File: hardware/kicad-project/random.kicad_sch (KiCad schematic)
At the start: 33 parts, among them J7 Conn_01x50, Q3 DMG2301L-7, SW1 K2-1109SP-C4SA, SW2 K2-1109SP-C4SA, SW3 K2-1109SP-C4SA, SW4 K2-1109SP-C4SA, SW5 GT-TC054C-H035-L1W, SW6 GT-TC054C-H035-L1W, SW7 GT-TC054C-H035-L1W

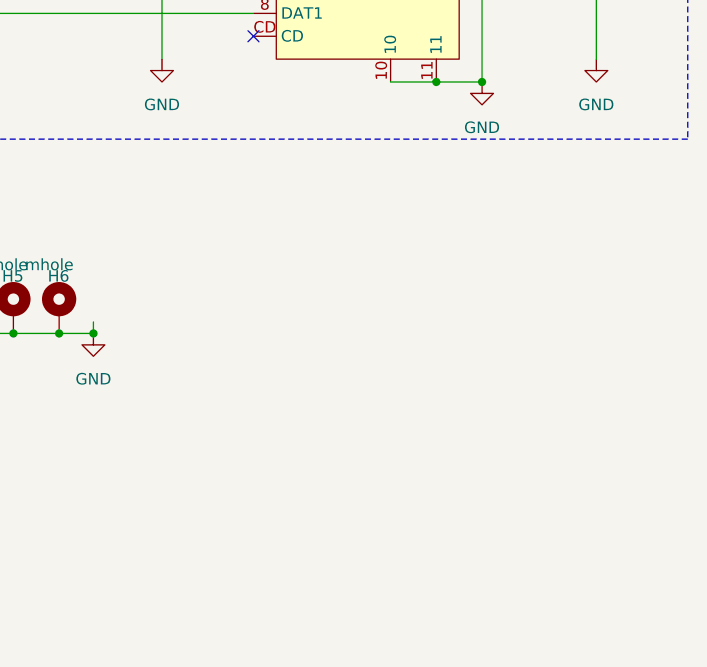
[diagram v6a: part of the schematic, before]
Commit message: change of LDO in schematics
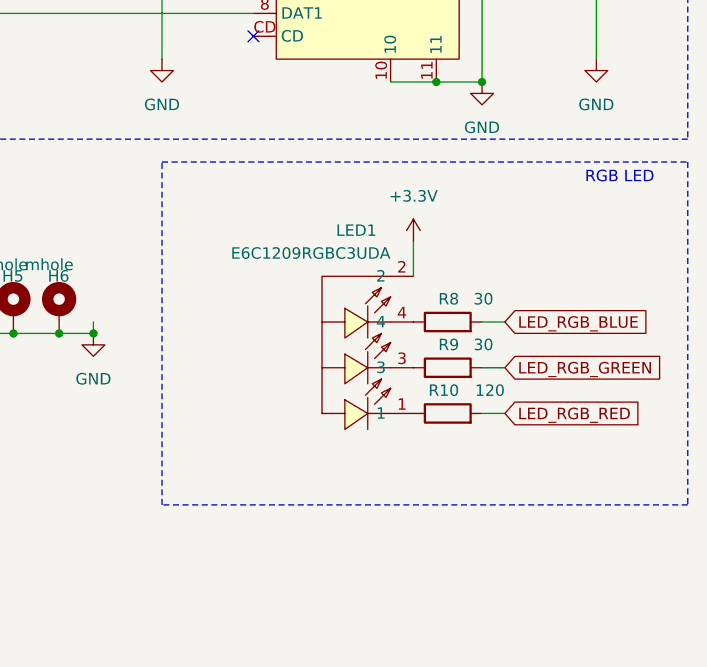
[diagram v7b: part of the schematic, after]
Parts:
- added LED1: E6C1209RGBC3UDA, easyeda2kicad:LED-ARRAY-SMD_4P-L3.2-W2.7-TL-1, symbol easyedaToKicad:E6C1209RGBC3UDA
- added R10: 120, Resistor_SMD:R_0805_2012Metric, symbol Device:R
- added R8, R9: 30, Resistor_SMD:R_0805_2012Metric, symbol Device:R
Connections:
- net +3.3V: now also LED1.2
- new net: LED1.4, R8.1
- new net: LED1.1, R10.1
- new net: LED1.3, R9.1
- new net LED_RGB_BLUE: R8.2
- new net LED_RGB_GREEN: R9.2
- new net LED_RGB_RED: R10.2
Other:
- note added: "RGB LED"
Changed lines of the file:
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@@
+    (stroke (width 0) (type default))
+  )
+  (wire (pts (xy 251.46 81.28) (xy 251.46 85.09))
     (stroke (width 0) (type default))
   )
@@
     (stroke (width 0) (type default))
   )
+  (wire (pts (xy 259.08 90.17) (xy 261.62 90.17))
+    (stroke (width 0) (type default))
+  )
   (wire (pts (xy 196.85 35.56) (xy 196.85 55.88))
     (stroke (width 0) (type default))
@@
   )
   (wire (pts (xy 223.52 60.96) (xy 223.52 50.8))
+    (stroke (width 0) (type default))
+  )
+  (wire (pts (xy 259.08 100.33) (xy 261.62 100.33))
     (stroke (width 0) (type default))
   )
@@
   )
   (wire (pts (xy 31.75 143.51) (xy 31.75 158.75))
+    (stroke (width 0) (type default))
+  )
+  (wire (pts (xy 259.08 95.25) (xy 261.62 95.25))
     (stroke (width 0) (type default))
   )
@@
     (fill (type none))
   )
+  (rectangle (start 223.52 72.39) (end 281.94 110.49)
+    (stroke (width 0) (type dash))
+    (fill (type none))
+  )
   (text "DB1" (at 106.68 125.73 0)
     (effects (font (size 1.27 1.27)) (justify left bottom))
@@
   )
   (text "DB0" (at 106.68 128.27 0)
+    (effects (font (size 1.27 1.27)) (justify left bottom))
+  )
+  (text "RGB LED\n" (at 270.51 74.93 0)
     (effects (font (size 1.27 1.27)) (justify left bottom))
   )
@@
     )
   )
+  (global_label "LED_RGB_RED" (shape input) (at 261.62 100.33 0) (fields_autoplaced)
+    (effects (font (size 1.27 1.27)) (justify left))
+    (property "Intersheetrefs" "${INTERSHEET_REFS}" (at 277.4865 100.33 0)
+      (effects (font (size 1.27 1.27)) (justify left) hide)
+    )
+  )
+  (global_label "LED_RGB_BLUE" (shape input) (at 261.62 90.17 0) (fields_autoplaced)
+    (effects (font (size 1.27 1.27)) (justify left))
+    (property "Intersheetrefs" "${INTERSHEET_REFS}" (at 278.5751 90.17 0)
+      (effects (font (size 1.27 1.27)) (justify left) hide)
+    )
+  )
   (global_label "SD_DAT_2" (shape input) (at 190.5 38.1 180) (fields_autoplaced)
     (effects (font (size 1.27 1.27)) (justify right))
@@
     )
   )
+  (global_label "LED_RGB_GREEN" (shape input) (at 261.62 95.25 0) (fields_autoplaced)
+    (effects (font (size 1.27 1.27)) (justify left))
+    (property "Intersheetrefs" "${INTERSHEET_REFS}" (at 279.966 95.25 0)
+      (effects (font (size 1.27 1.27)) (justify left) hide)
+    )
+  )
   (global_label "BTN_1" (shape input) (at 135.89 29.21 180) (fields_autoplaced)
     (effects (font (size 1.27 1.27)) (justify right))
@@
     )
   )
+  (symbol (lib_id "Device:R") (at 255.27 90.17 90) (unit 1)
+    (in_bom yes) (on_board yes) (dnp no)
+    (property "Reference" "R8" (at 256.54 87.63 90)
+      (effects (font (size 1.27 1.27)) (justify left))
+    )
+    (property "Value" "30" (at 260.35 87.63 90)
+      (effects (font (size 1.27 1.27)) (justify left))
+    )
+    (property "Footprint" "Resistor_SMD:R_0805_2012Metric" (at 255.27 91.948 90)
+      (effects (font (size 1.27 1.27)) hide)
+    )
+    (property "Datasheet" "~" (at 255.27 90.17 0)
+      (effects (font (size 1.27 1.27)) hide)
+    )
+    (pin "1")
+    (pin "2")
+    (instances
+      (project "Untitled"
+        (path "/0de5ae84-7f75-4a5a-83a1-35d27fd1d8d2"
+          (reference "R8") (unit 1)
+        )
+        (path "/0de5ae84-7f75-4a5a-83a1-35d27fd1d8d2/7a3aed0a-25fa-4aa7-ba6a-02a8683cfb94"
+          (reference "R8") (unit 1)
+        )
+      )
+    )
+  )
   (symbol (lib_id "Device:C") (at 52.07 52.07 0) (mirror x) (unit 1)
     (in_bom yes) (on_board yes) (dnp no)
@@
         (path "/0de5ae84-7f75-4a5a-83a1-35d27fd1d8d2/7a3aed0a-25fa-4aa7-ba6a-02a8683cfb94"
           (reference "#PWR019") (unit 1)
+        )
+      )
+    )
+  )
+  (symbol (lib_id "power:+3.3V") (at 251.46 81.28 0) (unit 1)
+    (in_bom yes) (on_board yes) (dnp no) (fields_autoplaced)
+    (property "Reference" "#PWR026" (at 251.46 85.09 0)
+      (effects (font (size 1.27 1.27)) hide)
+    )
+    (property "Value" "+3.3V" (at 251.46 76.2 0)
+      (effects (font (size 1.27 1.27)))
+    )
+    (property "Footprint" "" (at 251.46 81.28 0)
+      (effects (font (size 1.27 1.27)) hide)
+    )
+    (property "Datasheet" "" (at 251.46 81.28 0)
+      (effects (font (size 1.27 1.27)) hide)
+    )
+    (pin "1")
+    (instances
+      (project "Untitled"
+        (path "/0de5ae84-7f75-4a5a-83a1-35d27fd1d8d2"
+          (reference "#PWR026") (unit 1)
+        )
+        (path "/0de5ae84-7f75-4a5a-83a1-35d27fd1d8d2/7a3aed0a-25fa-4aa7-ba6a-02a8683cfb94"
+          (reference "#PWR026") (unit 1)
         )
       )
@@
         (path "/0de5ae84-7f75-4a5a-83a1-35d27fd1d8d2/7a3aed0a-25fa-4aa7-ba6a-02a8683cfb94"
           (reference "Q3") (unit 1)
+        )
+      )
+    )
+  )
+  (symbol (lib_id "Device:R") (at 255.27 100.33 90) (unit 1)
+    (in_bom yes) (on_board yes) (dnp no)
+    (property "Reference" "R10" (at 256.54 97.79 90)
+      (effects (font (size 1.27 1.27)) (justify left))
+    )
+    (property "Value" "120" (at 261.62 97.79 90)
+      (effects (font (size 1.27 1.27)) (justify left))
+    )
+    (property "Footprint" "Resistor_SMD:R_0805_2012Metric" (at 255.27 102.108 90)
+      (effects (font (size 1.27 1.27)) hide)
+    )
+    (property "Datasheet" "~" (at 255.27 100.33 0)
+      (effects (font (size 1.27 1.27)) hide)
+    )
+    (pin "1")
+    (pin "2")
+    (instances
+      (project "Untitled"
+        (path "/0de5ae84-7f75-4a5a-83a1-35d27fd1d8d2"
+          (reference "R10") (unit 1)
+        )
+        (path "/0de5ae84-7f75-4a5a-83a1-35d27fd1d8d2/7a3aed0a-25fa-4aa7-ba6a-02a8683cfb94"
+          (reference "R10") (unit 1)
         )
       )
@@
     )
   )
+  (symbol (lib_id "easyedaToKicad:E6C1209RGBC3UDA") (at 246.38 95.25 90) (unit 1)
+    (in_bom yes) (on_board yes) (dnp no)
+    (property "Reference" "LED1" (at 245.11 80.01 90)
+      (effects (font (size 1.27 1.27)))
+    )
+    (property "Value" "E6C1209RGBC3UDA" (at 240.03 82.55 90)
+      (effects (font (size 1.27 1.27)))
+    )
+    (property "Footprint" "easyeda2kicad:LED-ARRAY-SMD_4P-L3.2-W2.7-TL-1" (at 259.08 95.25 0)
+      (effects (font (size 1.27 1.27)) hide)
+    )
+    (property "Datasheet" "https://lcsc.com/product-detail/Light-Emitting-Diodes-LED_EKINGLUX-E6C1209RGBC3UDA_C375572.html" (at 261.62 95.25 0)
+      (effects (font (size 1.27 1.27)) hide)
+    )
+    (property "LCSC Part" "C375572" (at 264.16 95.25 0)
+      (effects (font (size 1.27 1.27)) hide)
+    )
+    (pin "1")
+    (pin "2")
+    (pin "3")
+    (pin "4")
+    (instances
+      (project "Untitled"
+        (path "/0de5ae84-7f75-4a5a-83a1-35d27fd1d8d2"
+          (reference "LED1") (unit 1)
+        )
+        (path "/0de5ae84-7f75-4a5a-83a1-35d27fd1d8d2/7a3aed0a-25fa-4aa7-ba6a-02a8683cfb94"
+          (reference "LED1") (unit 1)
+        )
+      )
+    )
+  )
   (symbol (lib_id "Device:C") (at 271.78 38.1 0) (mirror x) (unit 1)
     (in_bom yes) (on_board yes) (dnp no)
@@
         )
       )
+    )
+  )
+  (symbol (lib_id "Device:R") (at 255.27 95.25 90) (unit 1)
+    (in_bom yes) (on_board yes) (dnp no)
+    (property "Reference" "R9" (at 256.54 92.71 90)
+      (effects (font (size 1.27 1.27)) (justify left))
+    )
+    (property "Value" "30" (at 260.35 92.71 90)
+      (effects (font (size 1.27 1.27)) (justify left))
+    )
+    (property "Footprint" "Resistor_SMD:R_0805_2012Metric" (at 255.27 97.028 90)
+      (effects (font (size 1.27 1.27)) hide)
+    )
+    (property "Datasheet" "~" (at 255.27 95.25 0)
+      (effects (font (size 1.27 1.27)) hide)
+    )
+    (pin "1")
+    (pin "2")
+    (instances
+      (project "Untitled"
+        (path "/0de5ae84-7f75-4a5a-83a1-35d27fd1d8d2"
+          (reference "R9") (unit 1)
+        )
+        (path "/0de5ae84-7f75-4a5a-83a1-35d27fd1d8d2/7a3aed0a-25fa-4aa7-ba6a-02a8683cfb94"
+          (reference "R9") (unit 1)
+        )
+      )
